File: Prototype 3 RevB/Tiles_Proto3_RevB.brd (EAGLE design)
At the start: 46 x 46 mm, 63 parts, among them Q1 DMG3415U-7, T2 MMBT3904, U1 MDBT42Q, U2 AP2112, U3 ADXL345, U4 CAP1188, U5 DRV2605L, X1 32.768

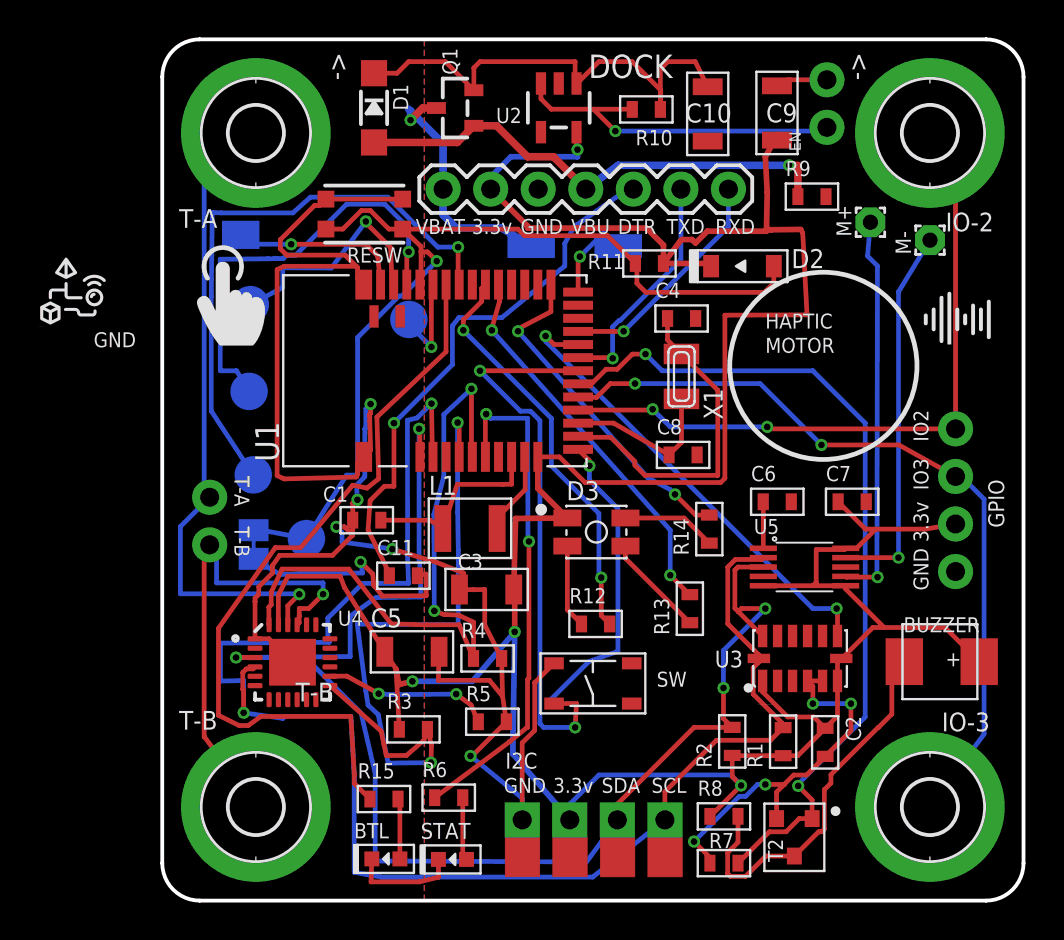
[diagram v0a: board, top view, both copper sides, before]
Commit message: sent to production
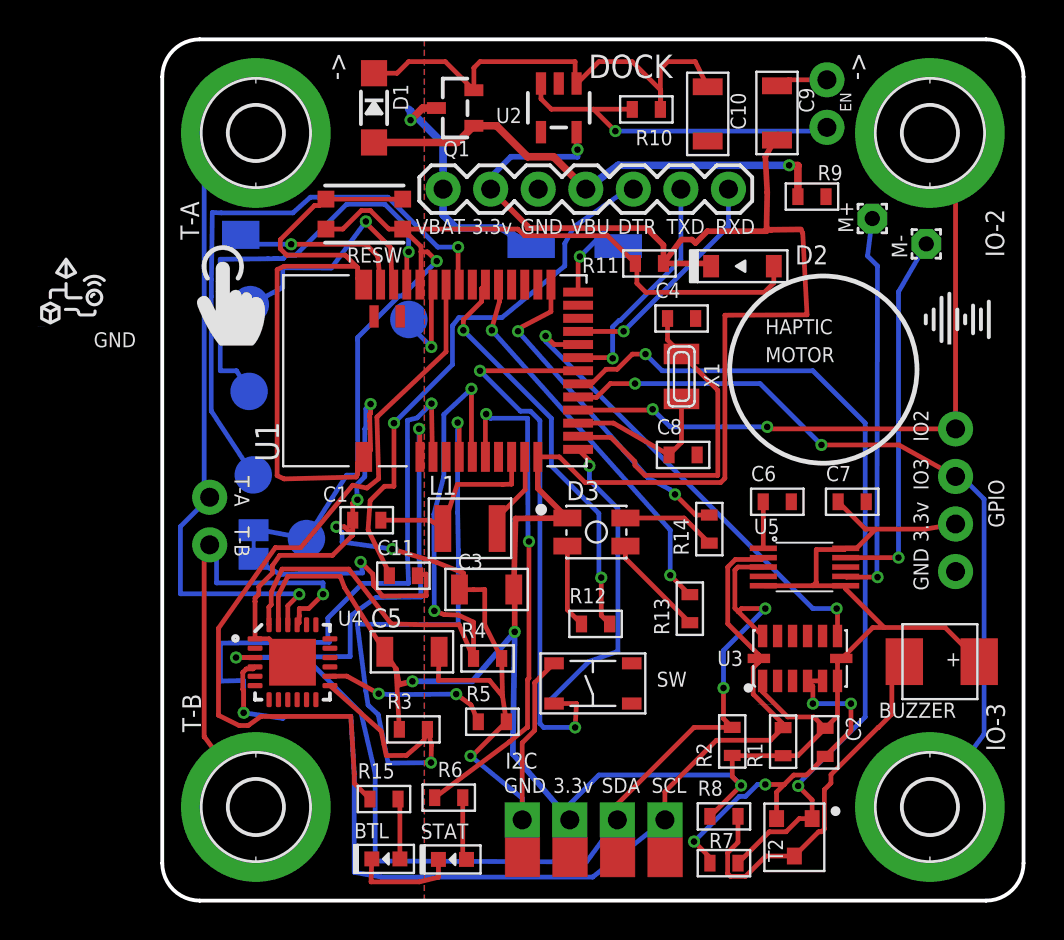
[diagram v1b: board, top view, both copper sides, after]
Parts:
- moved M- 0.28 mm to (40.8, -10.9)
- moved M+ 0.22 mm to (37.9, -9.57)
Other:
- board text added: "BATTERY"
- board text added: "Tiles IoT Toolkit"
- board text removed: "tilestoolkit.io"
